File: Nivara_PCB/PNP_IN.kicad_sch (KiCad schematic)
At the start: 6 parts, among them U15 LTV-357T, U16 LTV-357T

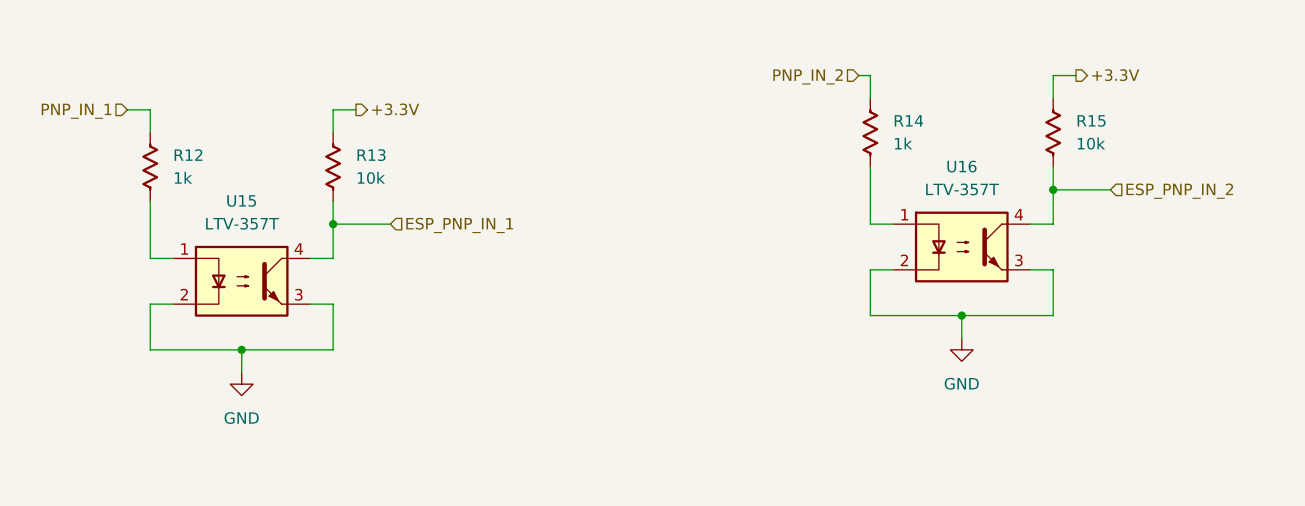
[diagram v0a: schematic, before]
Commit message: Cambios en la medición de voltaje y corriente de la PCB Nivara.
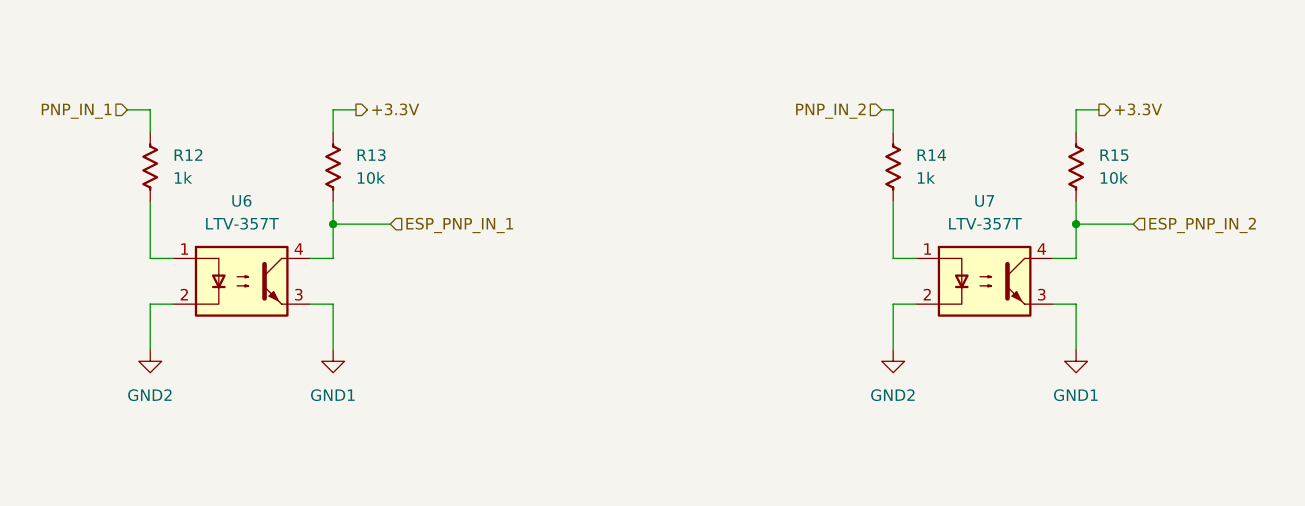
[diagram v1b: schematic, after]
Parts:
- renumbered U15 to U6, U16 to U7
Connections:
- net GND renamed GND1
- net GND1: no longer U6.2, U7.2
- new net GND2: U6.2, U7.2
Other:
- moved on the sheet: R14, R15, U7

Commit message: New changes to the Nivara PCB schematic files.
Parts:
- added D24, D25: LED ON, LED_SMD:LED_0603_1608Metric, symbol Device:LED
- R13, R15: value 10k -> 140
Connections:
- net ESP_PNP_IN_1: now also D24.1 (K); no longer R13.2
- net ESP_PNP_IN_2: now also D25.1 (K); no longer R15.2
- new net: D25.2 (A), R15.2
- new net: D24.2 (A), R13.2
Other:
- moved on the sheet: R13

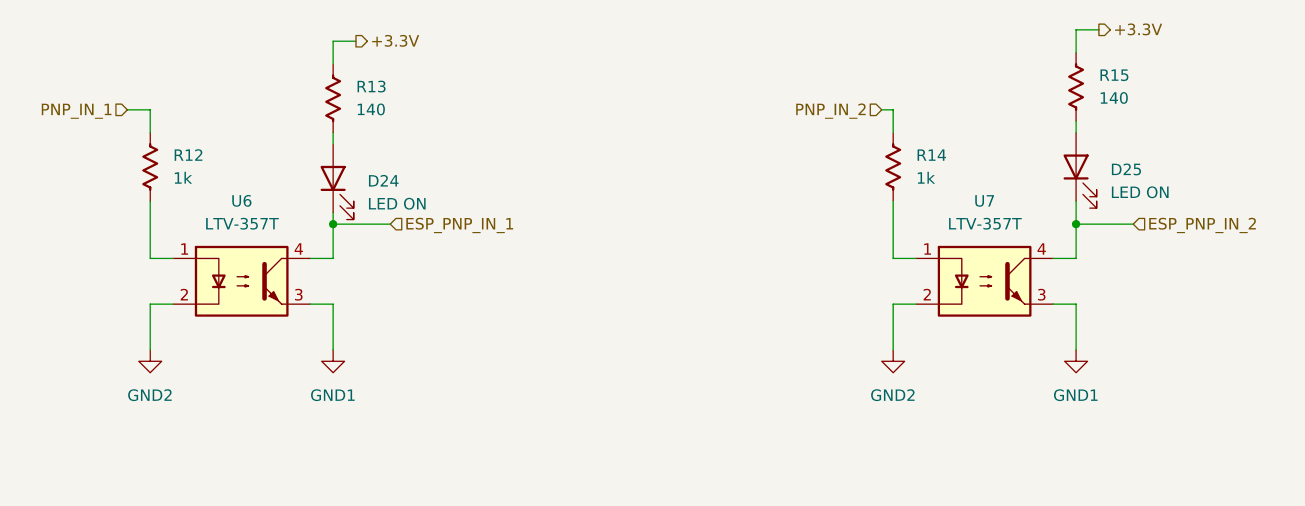
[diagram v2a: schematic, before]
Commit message: Cambios en el PCB de Nivara. Ruteo de emtradas y salidas NPN y PNP.
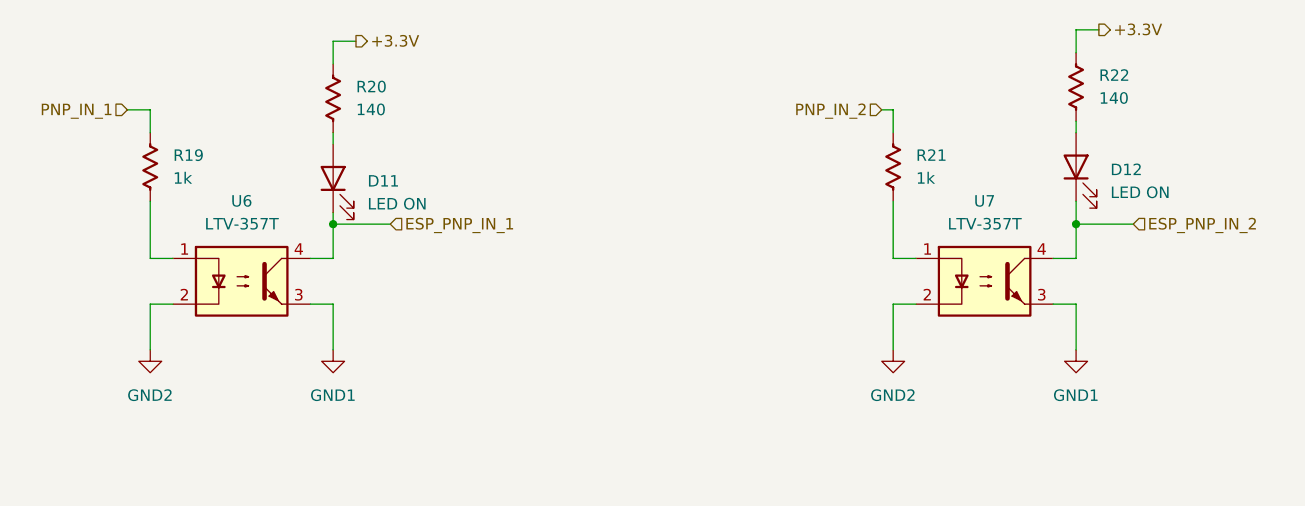
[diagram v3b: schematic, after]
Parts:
- removed R14: 1k, PCM_Resistor_SMD_AKL:R_0603_1608Metric, symbol PCM_Resistor_US_AKL:R_0603
- added R21: 1k, PCM_Resistor_SMD_AKL:R_0603_1608Metric, symbol PCM_Resistor_US_AKL:R_0603
- renumbered D24 to D11, D25 to D12, R12 to R19, R13 to R20, R15 to R22
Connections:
- net PNP_IN_2: now also R21.1
- net at U7.1: now also R21.2
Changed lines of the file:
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@@
 		(dnp no)
 		(fields_autoplaced yes)
-		(property "Reference" "#PWR031"
+		(property "Reference" "#PWR052"
 			(at 162.56 100.33 0)
 			(effects
@@
 			(project "Nivara_PCB"
 				(path "/13184db0-a71d-4054-b13a-bbf46d2b100d/4e7fa7f2-8bf5-4f9c-874d-fa1b4fd76f92/48f5ac7a-6bba-49c0-99bb-db418c675091"
-					(reference "#PWR031")
+					(reference "#PWR052")
 					(unit 1)
 				)
@@
 		(dnp no)
 		(fields_autoplaced yes)
-		(property "Reference" "D25"
+		(property "Reference" "D12"
 			(at 186.69 73.9774 90)
 			(effects
@@
 			(project "Nivara_PCB"
 				(path "/13184db0-a71d-4054-b13a-bbf46d2b100d/4e7fa7f2-8bf5-4f9c-874d-fa1b4fd76f92/48f5ac7a-6bba-49c0-99bb-db418c675091"
-					(reference "D25")
+					(reference "D12")
+					(unit 1)
+				)
+			)
+		)
+	)
+	(symbol
+		(lib_id "PCM_Resistor_US_AKL:R_0603")
+		(at 162.56 73.66 0)
+		(unit 1)
+		(exclude_from_sim no)
+		(in_bom yes)
+		(on_board yes)
+		(dnp no)
+		(fields_autoplaced yes)
+		(property "Reference" "R21"
+			(at 165.1 72.3899 0)
+			(effects
+				(font
+					(size 1.27 1.27)
+				)
+				(justify left)
+			)
+		)
+		(property "Value" "1k"
+			(at 165.1 74.9299 0)
+			(effects
+				(font
+					(size 1.27 1.27)
+				)
+				(justify left)
+			)
+		)
+		(property "Footprint" "PCM_Resistor_SMD_AKL:R_0603_1608Metric"
+			(at 162.56 85.09 0)
+			(effects
+				(font
+					(size 1.27 1.27)
+				)
+				(hide yes)
+			)
+		)
+		(property "Datasheet" "~"
+			(at 162.56 73.66 0)
+			(effects
+				(font
+					(size 1.27 1.27)
+				)
+				(hide yes)
+			)
+		)
+		(property "Description" "SMD 0603 Chip Resistor, US Symbol, Alternate KiCad Library"
+			(at 162.56 73.66 0)
+			(effects
+				(font
+					(size 1.27 1.27)
+				)
+				(hide yes)
+			)
+		)
+		(pin "2"
+		)
+		(pin "1"
+		)
+		(instances
+			(project "Nivara_PCB"
+				(path "/13184db0-a71d-4054-b13a-bbf46d2b100d/4e7fa7f2-8bf5-4f9c-874d-fa1b4fd76f92/48f5ac7a-6bba-49c0-99bb-db418c675091"
+					(reference "R21")
 					(unit 1)
 				)
@@
 		(dnp no)
 		(fields_autoplaced yes)
-		(property "Reference" "R12"
+		(property "Reference" "R19"
 			(at 82.55 72.3899 0)
 			(effects
@@
 			(project "Nivara_PCB"
 				(path "/13184db0-a71d-4054-b13a-bbf46d2b100d/4e7fa7f2-8bf5-4f9c-874d-fa1b4fd76f92/48f5ac7a-6bba-49c0-99bb-db418c675091"
-					(reference "R12")
+					(reference "R19")
 					(unit 1)
 				)
@@
 		(dnp no)
 		(fields_autoplaced yes)
-		(property "Reference" "#PWR029"
+		(property "Reference" "#PWR050"
 			(at 80.01 100.33 0)
 			(effects
@@
 			(project "Nivara_PCB"
 				(path "/13184db0-a71d-4054-b13a-bbf46d2b100d/4e7fa7f2-8bf5-4f9c-874d-fa1b4fd76f92/48f5ac7a-6bba-49c0-99bb-db418c675091"
-					(reference "#PWR029")
+					(reference "#PWR050")
 					(unit 1)
 				)
@@
 		(dnp no)
 		(fields_autoplaced yes)
-		(property "Reference" "R13"
+		(property "Reference" "R20"
 			(at 102.87 64.7699 0)
 			(effects
@@
 			(project "Nivara_PCB"
 				(path "/13184db0-a71d-4054-b13a-bbf46d2b100d/4e7fa7f2-8bf5-4f9c-874d-fa1b4fd76f92/48f5ac7a-6bba-49c0-99bb-db418c675091"
-					(reference "R13")
-					(unit 1)
-				)
-			)
-		)
-	)
-	(symbol
-		(lib_id "PCM_Resistor_US_AKL:R_0603")
-		(at 162.56 73.66 0)
-		(unit 1)
-		(exclude_from_sim no)
-		(in_bom yes)
-		(on_board yes)
-		(dnp no)
-		(fields_autoplaced yes)
-		(property "Reference" "R14"
-			(at 165.1 72.3899 0)
-			(effects
-				(font
-					(size 1.27 1.27)
-				)
-				(justify left)
-			)
-		)
-		(property "Value" "1k"
-			(at 165.1 74.9299 0)
-			(effects
-				(font
-					(size 1.27 1.27)
-				)
-				(justify left)
-			)
-		)
-		(property "Footprint" "PCM_Resistor_SMD_AKL:R_0603_1608Metric"
-			(at 162.56 85.09 0)
-			(effects
-				(font
-					(size 1.27 1.27)
-				)
-				(hide yes)
-			)
-		)
-		(property "Datasheet" "~"
-			(at 162.56 73.66 0)
-			(effects
-				(font
-					(size 1.27 1.27)
-				)
-				(hide yes)
-			)
-		)
-		(property "Description" "SMD 0603 Chip Resistor, US Symbol, Alternate KiCad Library"
-			(at 162.56 73.66 0)
-			(effects
-				(font
-					(size 1.27 1.27)
-				)
-				(hide yes)
-			)
-		)
-		(pin "2"
-		)
-		(pin "1"
-		)
-		(instances
-			(project "Nivara_PCB"
-				(path "/13184db0-a71d-4054-b13a-bbf46d2b100d/4e7fa7f2-8bf5-4f9c-874d-fa1b4fd76f92/48f5ac7a-6bba-49c0-99bb-db418c675091"
-					(reference "R14")
+					(reference "R20")
 					(unit 1)
 				)
@@
 		(dnp no)
 		(fields_autoplaced yes)
-		(property "Reference" "#PWR032"
+		(property "Reference" "#PWR053"
 			(at 182.88 100.33 0)
 			(effects
@@
 			(project "Nivara_PCB"
 				(path "/13184db0-a71d-4054-b13a-bbf46d2b100d/4e7fa7f2-8bf5-4f9c-874d-fa1b4fd76f92/48f5ac7a-6bba-49c0-99bb-db418c675091"
-					(reference "#PWR032")
+					(reference "#PWR053")
 					(unit 1)
 				)
@@
 		(dnp no)
 		(fields_autoplaced yes)
-		(property "Reference" "R15"
+		(property "Reference" "R22"
 			(at 185.42 63.4999 0)
 			(effects
@@
 			(project "Nivara_PCB"
 				(path "/13184db0-a71d-4054-b13a-bbf46d2b100d/4e7fa7f2-8bf5-4f9c-874d-fa1b4fd76f92/48f5ac7a-6bba-49c0-99bb-db418c675091"
-					(reference "R15")
+					(reference "R22")
 					(unit 1)
 				)
@@
 		(dnp no)
 		(fields_autoplaced yes)
-		(property "Reference" "D24"
+		(property "Reference" "D11"
 			(at 104.14 75.2474 90)
 			(effects
@@
 			(project "Nivara_PCB"
 				(path "/13184db0-a71d-4054-b13a-bbf46d2b100d/4e7fa7f2-8bf5-4f9c-874d-fa1b4fd76f92/48f5ac7a-6bba-49c0-99bb-db418c675091"
-					(reference "D24")
+					(reference "D11")
 					(unit 1)
 				)
@@
 		(dnp no)
 		(fields_autoplaced yes)
-		(property "Reference" "#PWR030"
+		(property "Reference" "#PWR051"
 			(at 100.33 100.33 0)
 			(effects
@@
 			(project "Nivara_PCB"
 				(path "/13184db0-a71d-4054-b13a-bbf46d2b100d/4e7fa7f2-8bf5-4f9c-874d-fa1b4fd76f92/48f5ac7a-6bba-49c0-99bb-db418c675091"
-					(reference "#PWR030")
-					(unit 1)
-				)
+					(reference "#PWR051")
+					(unit 1)
+				)

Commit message: Cambios realizados en el PCB y el esquema de Nivara_PCB.
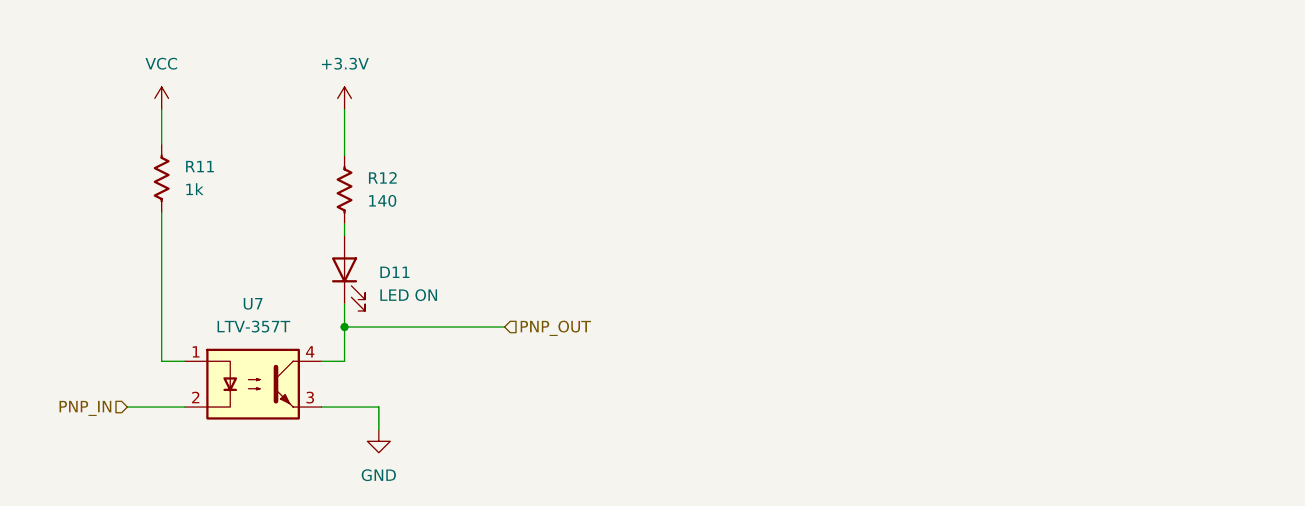
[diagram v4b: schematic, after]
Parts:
- removed D12: LED ON, LED_SMD:LED_0603_1608Metric, symbol Device:LED
- removed R19, R21: 1k, PCM_Resistor_SMD_AKL:R_0603_1608Metric, symbol PCM_Resistor_US_AKL:R_0603
- removed R20, R22: 140, PCM_Resistor_SMD_AKL:R_0603_1608Metric, symbol PCM_Resistor_US_AKL:R_0603
- removed U6: LTV-357T, Package_SO:SO-4_4.4x3.6mm_P2.54mm, symbol Isolator:LTV-357T
- added R11: 1k, PCM_Resistor_SMD_AKL:R_0603_1608Metric, symbol PCM_Resistor_US_AKL:R_0603
- added R12: 140, PCM_Resistor_SMD_AKL:R_0603_1608Metric, symbol PCM_Resistor_US_AKL:R_0603
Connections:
- net ESP_PNP_IN_2 is gone; now on net PNP_OUT: U7.4
- net +3.3V: now also R12.1
- net at U7.1: now also R11.2
- net at D11.2 (A): now also R12.2
- net ESP_PNP_IN_1 renamed PNP_OUT
- net GND1 renamed GND
- net GND2 renamed PNP_IN
- new net VCC: R11.1

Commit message: Cambios realizados en los archivos de Nivara_PCB.
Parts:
- D11: symbol Device:LED -> EasyEDA:LED
- R11, R12: symbol PCM_Resistor_US_AKL:R_0603 -> EasyEDA:R_0603
- U7: symbol Isolator:LTV-357T -> EasyEDA:LTV-357T
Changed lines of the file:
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@@
 	)
 	(symbol
-		(lib_id "power:VCC")
+		(lib_id "EasyEDA:VCC")
 		(at 81.28 67.31 0)
 		(unit 1)
@@
 	)
 	(symbol
-		(lib_id "power:+3.3V")
+		(lib_id "EasyEDA:+3.3V")
 		(at 101.6 67.31 0)
 		(unit 1)
@@
 	)
 	(symbol
-		(lib_id "PCM_Resistor_US_AKL:R_0603")
+		(lib_id "EasyEDA:R_0603")
 		(at 101.6 76.2 0)
 		(unit 1)
@@
 	)
 	(symbol
-		(lib_id "Isolator:LTV-357T")
+		(lib_id "EasyEDA:LTV-357T")
 		(at 91.44 97.79 0)
 		(unit 1)
@@
 	)
 	(symbol
-		(lib_id "Device:LED")
+		(lib_id "EasyEDA:LED")
 		(at 101.6 85.09 90)
 		(unit 1)
@@
 	)
 	(symbol
-		(lib_id "power:GND")
+		(lib_id "EasyEDA:GND")
 		(at 105.41 102.87 0)
 		(unit 1)
@@
 	)
 	(symbol
-		(lib_id "PCM_Resistor_US_AKL:R_0603")
+		(lib_id "EasyEDA:R_0603")
 		(at 81.28 74.93 0)
 		(unit 1)
